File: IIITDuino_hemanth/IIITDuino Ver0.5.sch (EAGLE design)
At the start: 86 parts, among them IC3 LM1117, J2 DCJ0202, M1 ELECTRET_MICROPHON-TOM-1545P-R, Q1 ZXMP6A13FTA, Q2 2N7002PW, T1 BC547, U1 FT231XS, U2 MIC5205, U4 ATMEGA328P_PDIP, Y1 16MHz

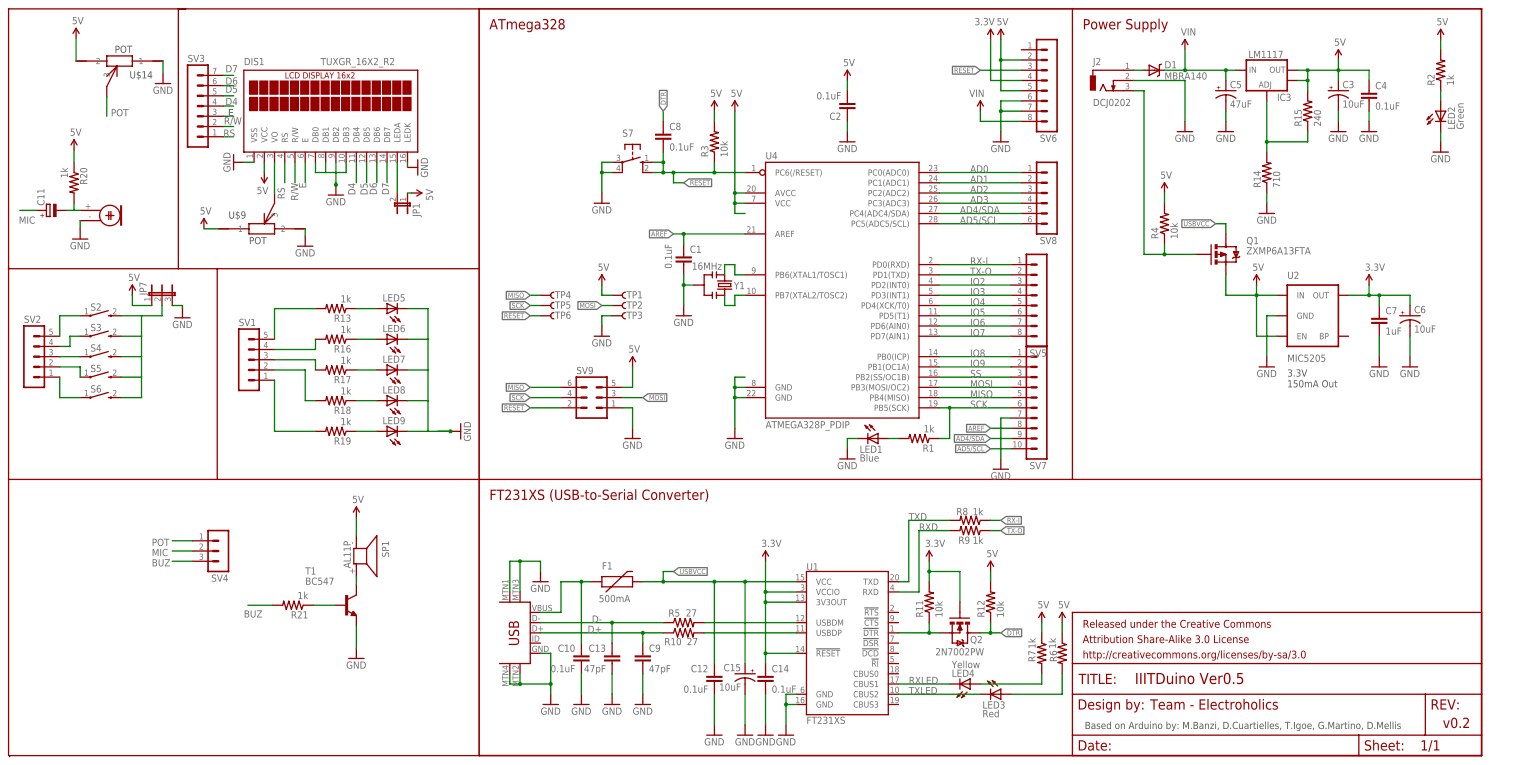
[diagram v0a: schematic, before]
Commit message: Seggregated the boards
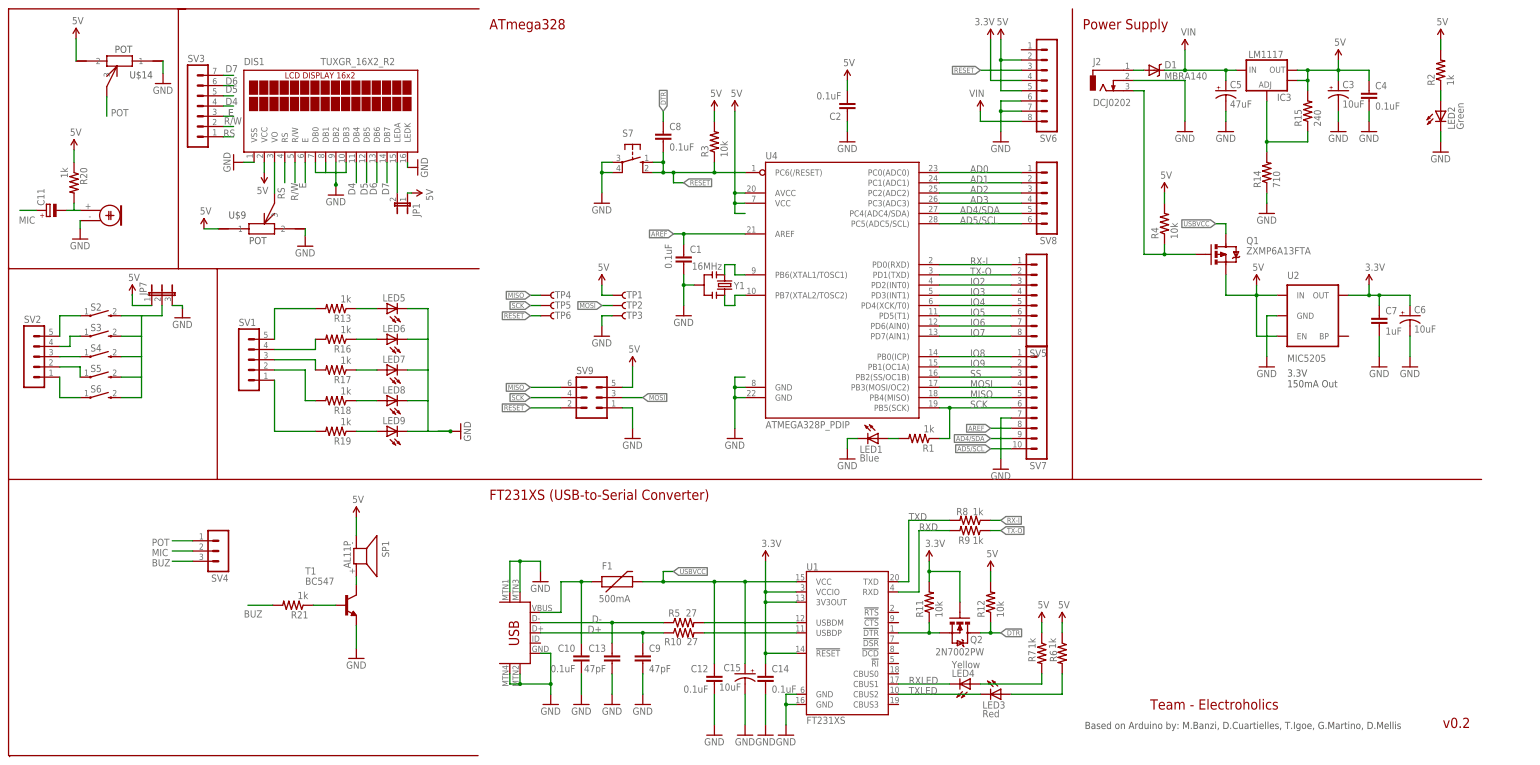
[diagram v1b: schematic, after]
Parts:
- removed FRAME2: FRAME-LETTER, SparkFun-Aesthetics:FRAME-LETTER
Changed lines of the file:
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@@
 <?xml version="1.0" encoding="utf-8"?>
 <!DOCTYPE eagle SYSTEM "eagle.dtd">
-<eagle version="7.5.0">
+<eagle version="9.1.2">
 <drawing>
 <settings>
 <setting alwaysvectorfont="no"/>
+<setting keepoldvectorfont="yes"/>
 <setting verticaltext="up"/>
 </settings>
@@
 <part name="GND10" library="SparkFun-Aesthetics" deviceset="GND" device=""/>
 <part name="GND20" library="SparkFun-Aesthetics" deviceset="GND" device=""/>
-<part name="FRAME2" library="SparkFun-Aesthetics" deviceset="FRAME-LETTER" device="">
-<attribute name="IIITDUINO" value=""/>
-</part>
 <part name="GND23" library="SparkFun-Aesthetics" deviceset="GND" device=""/>
 <part name="SUPPLY3" library="SparkFun-Aesthetics" deviceset="5V" device=""/>
@@
 <instance part="GND10" gate="1" x="66.04" y="5.08"/>
 <instance part="GND20" gate="1" x="58.42" y="5.08"/>
-<instance part="FRAME2" gate="G$1" x="0" y="0" smashed="yes"/>
-<instance part="FRAME2" gate="G$2" x="147.32" y="0" smashed="yes">
-<attribute name="LAST_DATE_TIME" x="160.02" y="1.27" size="2.54" layer="94" font="vector"/>
-<attribute name="SHEET" x="233.68" y="1.27" size="2.54" layer="94" font="vector"/>
-<attribute name="DRAWING_NAME" x="162.814" y="17.78" size="2.7432" layer="94" font="vector"/>
-</instance>
 <instance part="GND23" gate="1" x="129.54" y="152.4"/>
 <instance part="SUPPLY3" gate="G$1" x="129.54" y="177.8"/>
